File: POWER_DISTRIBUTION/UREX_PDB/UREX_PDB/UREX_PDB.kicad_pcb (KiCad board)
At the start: 4 copper layers, 90 x 60 mm, 114 parts, among them IC1 TCAN1044VDDFR, IC10 TPS22997RYZR, IC2 TPS1HB08BQPWPRQ1, IC3 TPS1HB08BQPWPRQ1, IC4 INA232AIDDFR, IC5 TCA6408ARGTR, IC8 TPS22997RYZR, IC9 TPS22997RYZR, J1 S2B-PH-SM4-TB_LF__SN_, J10 S2B-PH-SM4-TB_LF__SN_, J11 Conn_01x02, J33 Conn_01x02, J34 Conn_01x02, J36 Conn_01x02, J37 Conn_01x02, J4 S2B-PH-SM4-TB_LF__SN_, J5 S3B-PH-SM4-TB_LF__SN_, J6 S4B-PH-SM4-TB_LF__SN_, J7 S2B-PH-SM4-TB_LF__SN_, J8 S3B-PH-SM4-TB_LF__SN_, J9 S6B-PH-SM4-TB_LF__SN_, Q1 RSS070N05HZGTB, Q2 RSS070N05HZGTB, U1 ESP32-WROOM-32UE-R2, U7 USBLC6-2SC6

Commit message: added 5v 8A  dcdc
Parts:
- removed C1, C2, C3, C4, C5, C6, C7, C8: 10uF@16V, Capacitor_SMD:C_0805_2012Metric_Pad1.18x1.45mm_HandSolder
- removed PS1: TLV75733PDBVR, SamacSys_Parts:SOT95P280X145-5N
- removed PS5: RPMA5.0-4.5_OF, SamacSys_Parts:RPMA5045OF
- added C14: 330uF@50v, Capacitor_THT:CP_Radial_D10.0mm_P5.00mm, F.Cu at (121.6, 76.4)
- added C15: 10uF@50V, Capacitor_SMD:C_1210_3225Metric, F.Cu at (125.7, 84.1)
- added C16: 4.7uF, Capacitor_SMD:C_0805_2012Metric_Pad1.18x1.45mm_HandSolder, F.Cu at (128.4, 84.4)
- added C17: 4.7uF, Capacitor_SMD:C_0805_2012Metric_Pad1.18x1.45mm_HandSolder, F.Cu at (132.1, 75.9)
- added C19: 330pF, Capacitor_SMD:C_0603_1608Metric, F.Cu at (131.7, 91.9)
- added C20: 18nF, Capacitor_SMD:C_0603_1608Metric, F.Cu at (135.0, 91.9)
- added C21: 1uF, Capacitor_SMD:C_0805_2012Metric_Pad1.18x1.45mm_HandSolder, F.Cu at (123.0, 87.2)
- added C22: 47uF@16V, Capacitor_SMD:C_1210_3225Metric, F.Cu at (120.2, 86.8)
- added C36: 47uF@16V, Capacitor_SMD:C_1210_3225Metric, F.Cu at (116.8, 86.8)
- added C37: 47uF@16V, Capacitor_SMD:C_1210_3225Metric, F.Cu at (113.2, 86.8)
- added C38: 100nF @50V, Capacitor_SMD:C_0402_1005Metric_Pad0.74x0.62mm_HandSolder, F.Cu at (134.0, 86.7)
- added C39: 100nF @50V, Capacitor_SMD:C_0402_1005Metric_Pad0.74x0.62mm_HandSolder, F.Cu at (134.0, 83.9)
- added C40: 330uF@50v, Capacitor_THT:CP_Radial_D10.0mm_P5.00mm, F.Cu at (115.4, 94.6)
- added L1: XAL7070-472MEC, SamacSys_Parts:XAL7070472MEC, F.Cu at (139.5, 85.1)
- added R17: 301K, Resistor_SMD:R_0603_1608Metric, F.Cu at (139.1, 75.5)
- added R18: 100K, Resistor_SMD:R_0603_1608Metric, F.Cu at (137.4, 75.5)
- added R22: 102K, Resistor_SMD:R_0603_1608Metric, F.Cu at (134.0, 75.5)
- added R25: 16.9K, Resistor_SMD:R_0603_1608Metric, F.Cu at (133.4, 91.9)
- added R26: 48.7k, Resistor_SMD:R_0603_1608Metric, F.Cu at (130.2, 75.5)
- added R27: 102K, Resistor_SMD:R_0603_1608Metric, F.Cu at (135.7, 75.5)
- added R28: 100K, Resistor_SMD:R_0603_1608Metric, F.Cu at (127.2, 91.9)
- added R29: 31.6K, Resistor_SMD:R_0603_1608Metric, F.Cu at (129.0, 91.9)
- added U4: PLM1117120QDCYRQ1, LM1117120QDCYRQ1:SOT-223-4_DCY_TEX, F.Cu at (111.4, 80.0)
- added U5: XTPS552892RYQR, TPS552892RYQR:RYQ0021A-MFG, F.Cu at (131.6, 85.3)
- C12, C13, C25, C48, C49, C51, C53: value 100nF -> 100nF @50V
- C28, C29, C30, C31, C34, C35: footprint Capacitor_SMD:C_0805_2012Metric_Pad1.18x1.45mm_HandSolder -> Capacitor_SMD:C_0805_2012Metric
- C32: footprint Capacitor_SMD:C_1210_3225Metric_Pad1.33x2.70mm_HandSolder -> Capacitor_SMD:C_1210_3225Metric
- C47, IC4: moved to F.Cu
- R2: value R_Small -> 120r
- moved C51 20.0 mm to (103.5, 71.8)
- moved C52 19.9 mm to (103.5, 73.5)
- moved C18 19.1 mm to (108.8, 73.5)
- moved C25 16.1 mm to (108.8, 75.2)
- moved C12 15.5 mm to (109.8, 84.6), turned to 0 degrees
- moved C11 13.8 mm to (109.8, 86.4), turned to 0 degrees
- moved FB1 13.5 mm to (111.6, 74.3)
- moved C24 12.5 mm to (122.9, 93.9), turned to 0 degrees
- moved C23 9.31 mm to (122.9, 97.4), turned to 0 degrees
- moved IC1 8.54 mm to (103.5, 76.2), turned to 0 degrees
- moved C32 8.06 mm to (122.9, 100.8), turned to 0 degrees
- moved C47 4.72 mm to (135.0, 95.4)
- moved TP5 2.82 mm to (116.6, 76.3)
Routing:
- net /HighCurrentDCDC/DCDC_VCC: track 0.00 -> 14.8 mm, vias 0 -> 4
- net VBAT_Fused_OUT: track 19.1 -> 33.0 mm, vias 1 -> 41
- net Net-(U5-EN_UVLO): track 0.00 -> 10.4 mm
- net CAN_TX: track 30.6 -> 22.1 mm
- net Net-(U5-PG): track 0.00 -> 8.41 mm
- net Net-(U5-FSW): track 0.00 -> 8.29 mm
- net Net-(U5-CC_N): track 0.00 -> 7.90 mm
- net CAN+: track 6.06 -> 13.5 mm
- net CAN-: track 6.06 -> 12.8 mm
- net /HighCurrentDCDC/DCDC_FB: track 0.00 -> 6.48 mm
- net +3V3: track 48.5 -> 54.0 mm, vias 34 -> 26
- net /HighCurrentDCDC/COMP: track 0.00 -> 5.25 mm
- net Net-(U5-SW2): track 0.00 -> 2.58 mm
- net Net-(U5-SW1): track 0.00 -> 2.57 mm
- net VBAT_Fused: track 25.4 -> 23.3 mm, vias 50 -> 49
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- added copper zone on In1.Cu, net +5V0
- added copper zone on F.Cu, net Net-(U5-SW1)
- added copper zone on F.Cu, net Net-(U5-SW2)
- added copper zone on In1.Cu, net VBAT_Fused_OUT
- removed copper zone on B.Cu, net +3V3
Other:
- board text removed: "3V3 TP"

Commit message: V1 Full Fabrication(Freezed design)
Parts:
- removed J1: S2B-PH-SM4-TB_LF__SN_, SamacSys_Parts:S2BPHSM4TBLFSN
- added J12: S3B-PH-SM4-TB_LF__SN_, SamacSys_Parts:S3BPHSM4TBLFSN, B.Cu at (110.2, 69.5)
- C20: value 18nF -> 22nF
- C28, C29, C34: value 1uF @50V -> 1nF; footprint Capacitor_SMD:C_0805_2012Metric -> Capacitor_SMD:C_0603_1608Metric
- H5, H7, H8: footprint MountingHole:MountingHole_2.2mm_M2_ISO7380_Pad -> MountingHole:MountingHole_2.2mm_M2_ISO7380
- H6: footprint MountingHole:MountingHole_2.2mm_M2_ISO7380_Pad -> MountingHole:MountingHole_2.2mm_M2_Pad_Via
- TP2, TP3, TP4, TP5, TP6, TP7: footprint TestPoint:TestPoint_Pad_1.5x1.5mm -> TestPoint:TestPoint_Pad_D1.0mm
- TP8: footprint TestPoint:TestPoint_Pad_1.5x1.5mm -> TestPoint:TestPoint_Pad_D1.0mm; moved to F.Cu
- moved TP2 15.3 mm to (167.7, 110.5)
- moved C11 12.2 mm to (117.9, 77.3), turned to 90 degrees
- moved C12 9.68 mm to (116.1, 77.3), turned to 90 degrees
- moved TP5 9.17 mm to (108.5, 72.0), turned to 180 degrees
- moved C52 7.29 mm to (97.2, 77.2), turned to -90 degrees
- moved C51 7.11 mm to (99.0, 77.2), turned to -90 degrees
- moved C18 6.15 mm to (105.0, 78.3), turned to -90 degrees
- moved FB1 4.92 mm to (106.7, 74.8)
- moved U4 4.30 mm to (111.5, 75.7), turned to 0 degrees
- moved C25 3.70 mm to (106.7, 78.3), turned to -90 degrees
- moved R62 3.38 mm to (88.6, 74.4)
- moved S1 3.38 mm to (84.7, 72.2)
- moved J9 1.51 mm to (93.9, 115.2)
- moved R28 1.33 mm to (127.1, 90.6)
- moved IC1 1.32 mm to (102.2, 76.7)
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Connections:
- C10 pad 2: VBAT+ -> VBAT_Fused_OUT
- C11 pad 1: +5V0 -> VBAT_Fused_OUT
- C12 pad 1: +5V0 -> VBAT_Fused_OUT
- C9 pad 2: VBAT+ -> VBAT_Fused_OUT
- IC2 pad 17: VBAT+ -> VBAT_Fused_OUT
- IC3 pad 17: VBAT+ -> VBAT_Fused_OUT
- J33 pad 1: VBAT_Fused -> VBAT_Fused_OUT
- J34 pad 1: VBAT_Fused -> VBAT_Fused_OUT
- R19 pad 1: +3V3 -> 5VDC_BUS1
- R20 pad 1: +3V3 -> 5VDC_BUS2
- R21 pad 1: +3V3 -> Net-(IC10-PG)
- R21 pad 2: Net-(IC10-PG) -> 5VDC_BUS3
- U4 pad 3: +5V0 -> VBAT_Fused_OUT
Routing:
- net 5VDC_BUS1: track 6.69 -> 19.8 mm, vias 0 -> 2
- net GND: track 76.8 -> 86.8 mm, vias 141 -> 159
- net 5VDC_BUS2: track 2.14 -> 10.1 mm, vias 0 -> 1
- net VBAT_Fused_OUT: track 33.0 -> 25.5 mm, vias 41 -> 77
- net /HighCurrentDCDC/DCDC_VCC: track 14.8 -> 21.5 mm
- net 5VDC_BUS3: track 0.07 -> 5.99 mm, vias 0 -> 2
- net VBAT_Fused: track 23.3 -> 18.4 mm, vias 49 -> 0
- net I2C2_SDL: track 53.4 -> 57.3 mm, vias 3 -> 2
- net +3V3: track 54.0 -> 50.6 mm
- net BOOT: track 33.1 -> 29.8 mm
- net VTX_EN_EXT: track 17.1 -> 14.5 mm
- net CAN_TX: track 22.1 -> 20.0 mm
- net Net-(IC10-PG): track 2.34 -> 4.23 mm, vias 0 -> 1
- net VTX_EN: track 105.7 -> 107.3 mm
- net +5V0: track 1.64 -> 0.00 mm
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- removed copper zone on In1.Cu, net VBAT+
- removed copper zone on B.Cu, net VBAT_Fused
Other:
- board size 90 x 60 mm -> 89.8 x 59.7 mm
- board text added: "VBAT"

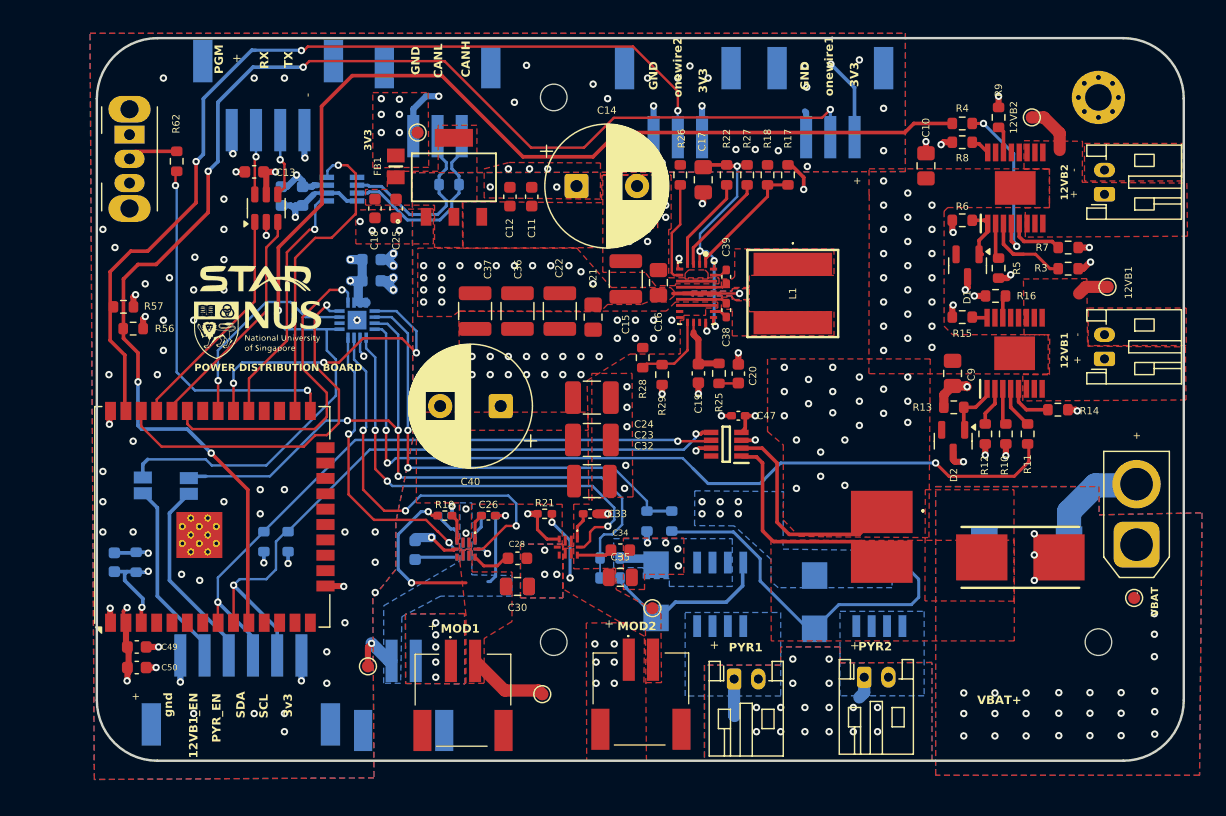
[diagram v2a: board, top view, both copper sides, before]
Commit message: fixed jarring pcb issues
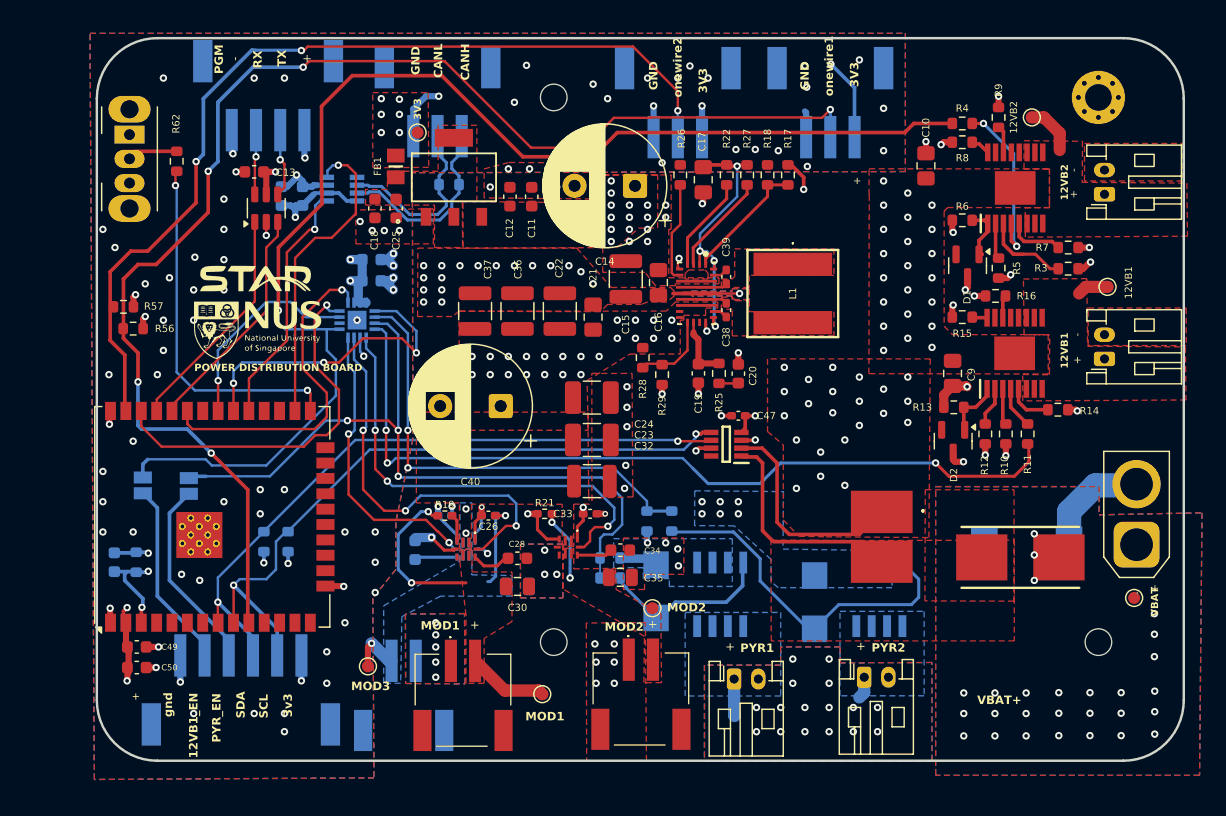
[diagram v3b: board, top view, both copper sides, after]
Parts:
- moved C14 4.84 mm to (126.5, 76.4), turned to 180 degrees
- turned C26 to 0 degrees
- turned C27 to 0 degrees
- turned C33 to 0 degrees
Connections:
- C14 pad 1: GND -> VBAT_Fused_OUT
- C14 pad 2: VBAT_Fused_OUT -> GND
- C26 pad 2: Net-(IC8-VBIAS) -> GND
- C27 pad 2: Net-(IC9-VBIAS) -> GND
- C33 pad 2: Net-(IC10-VBIAS) -> GND
- IC10 pad 1: Net-(IC10-VBIAS) -> +3V3
- IC8 pad 1: Net-(IC8-VBIAS) -> +3V3
- IC9 pad 1: Net-(IC9-VBIAS) -> +3V3
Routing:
- net +3V3: track 50.6 -> 57.4 mm
- net Net-(IC9-VBIAS): track 2.88 -> 0.00 mm
- net GND: track 86.8 -> 89.1 mm, vias 159 -> 162
- net Net-(IC8-VBIAS): track 2.32 -> 0.00 mm
- net Net-(IC10-VBIAS): track 2.29 -> 0.00 mm
